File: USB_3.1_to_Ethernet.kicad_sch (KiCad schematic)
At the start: 5 parts, among them J1 RJ45_JK0654219, U1 LAN7801_9JX, U2 93LC56B_SN, U3 KSZ9031RNXCC, Y1 C3E-8.000-18-3030-R

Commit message: power section added and power conections made
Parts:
- Y1: value C3E-8.000-18-3030-R -> 125MHz
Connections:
- net DVDDH is gone; now on net AVDDH: U3.16 (DVDDH), U3.34 (DVDDH), U3.40 (DVDDH)
- net DVDDL is gone; now on net AVDDL: U3.14 (DVDDL), U3.18 (DVDDL), U3.23 (DVDDL), U3.26 (DVDDL), U3.30 (DVDDL), U3.39 (DVDDL)
- net P_GND is gone; now on net GND: U3.49 (P_GND), U3.49_1 (P_GND), U3.49_10 (P_GND), U3.49_11 (P_GND), U3.49_12 (P_GND), U3.49_13 (P_GND), U3.49_14 (P_GND), U3.49_15 (P_GND), U3.49_16 (P_GND), U3.49_17 (P_GND), U3.49_18 (P_GND), U3.49_19 (P_GND), U3.49_2 (P_GND), U3.49_20 (P_GND), U3.49_21 (P_GND), U3.49_22 (P_GND), U3.49_23 (P_GND), U3.49_24 (P_GND), U3.49_25 (P_GND), U3.49_3 (P_GND), U3.49_4 (P_GND), U3.49_5 (P_GND), U3.49_6 (P_GND), U3.49_7 (P_GND), U3.49_8 (P_GND), U3.49_9 (P_GND)
- net VDDVARIO is gone; now on net AVDDH: U1.11 (VDDVARIO), U1.18 (VDDVARIO), U1.27 (VDDVARIO), U1.3 (VDDVARIO), U1.48 (VDDVARIO), U1.51 (VDDVARIO), U1.7 (VDDVARIO)
- net AVDDH: now also U1.21 (VDD_SW_IN), U1.50 (VDD33A), U1.64 (VDD33_REG_IN)
- net GND: now also U1.65 (VSS), U3.29 (VSS)
- net XI: now reaches Y1.1
- net XI: now also U1.52 (XI)
- net XO: now reaches Y1.3
- net XO: now also U1.53 (XO)
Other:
- moved on the sheet: U1, Y1

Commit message: usb connections done without 27 ohm, SMI connections done, EEPROM connections done.
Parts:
- added R1: 12K, Resistor_SMD:R_0201_0603Metric_Pad0.64x0.40mm_HandSolder, symbol Device:R
- added R2, R3: 1.5K, Resistor_SMD:R_1206_3216Metric, symbol Device:R
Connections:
- net AVDDH: now also U2.8 (VCC), R2.1, R3.1
- net GND: now also U2.5 (VSS), R1.2
- net CS: now reaches U2.1 (CS)
- net CS: now also U1.23 (EECS/GPIO0)
- net CLK: now reaches U2.2 (CLK)
- net CLK: now also U1.26 (EECLK/GPIO3)
- net DI: now reaches U2.3 (DI)
- net DI: now also U1.24 (EEDI/GPIO1)
- net DO: now reaches U2.4 (DO)
- net DO: now also U1.25 (EEDO/GPIO2)
- net MDC: now reaches U3.36 (MDC)
- net MDC: now also U1.56 (MDC), R2.2
- net MDIO: now reaches U3.37 (MDIO)
- net MDIO: now also U1.55 (MDIO), R3.2
- net D+: now reaches U1.38 (USB2_DP)
- net D-: now reaches U1.39 (USB2_DM)
- net SSTX+: now reaches U1.40 (USB3_TXDP)
- net SSTX-: now reaches U1.41 (USB3_TXDM)
- net SSRX+: now reaches U1.43 (USB3_RXDP)
- net SSRX-: now reaches U1.44 (USB3_RXDM)
- net at U1.49 (USBRBIAS): now also R1.1
- no-connect marks 0 -> 1
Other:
- note added: "Gigabit Ethernet MAC"
- note added: "clk circuitry"
- moved on the sheet: J1, U1, U2, U3, Y1

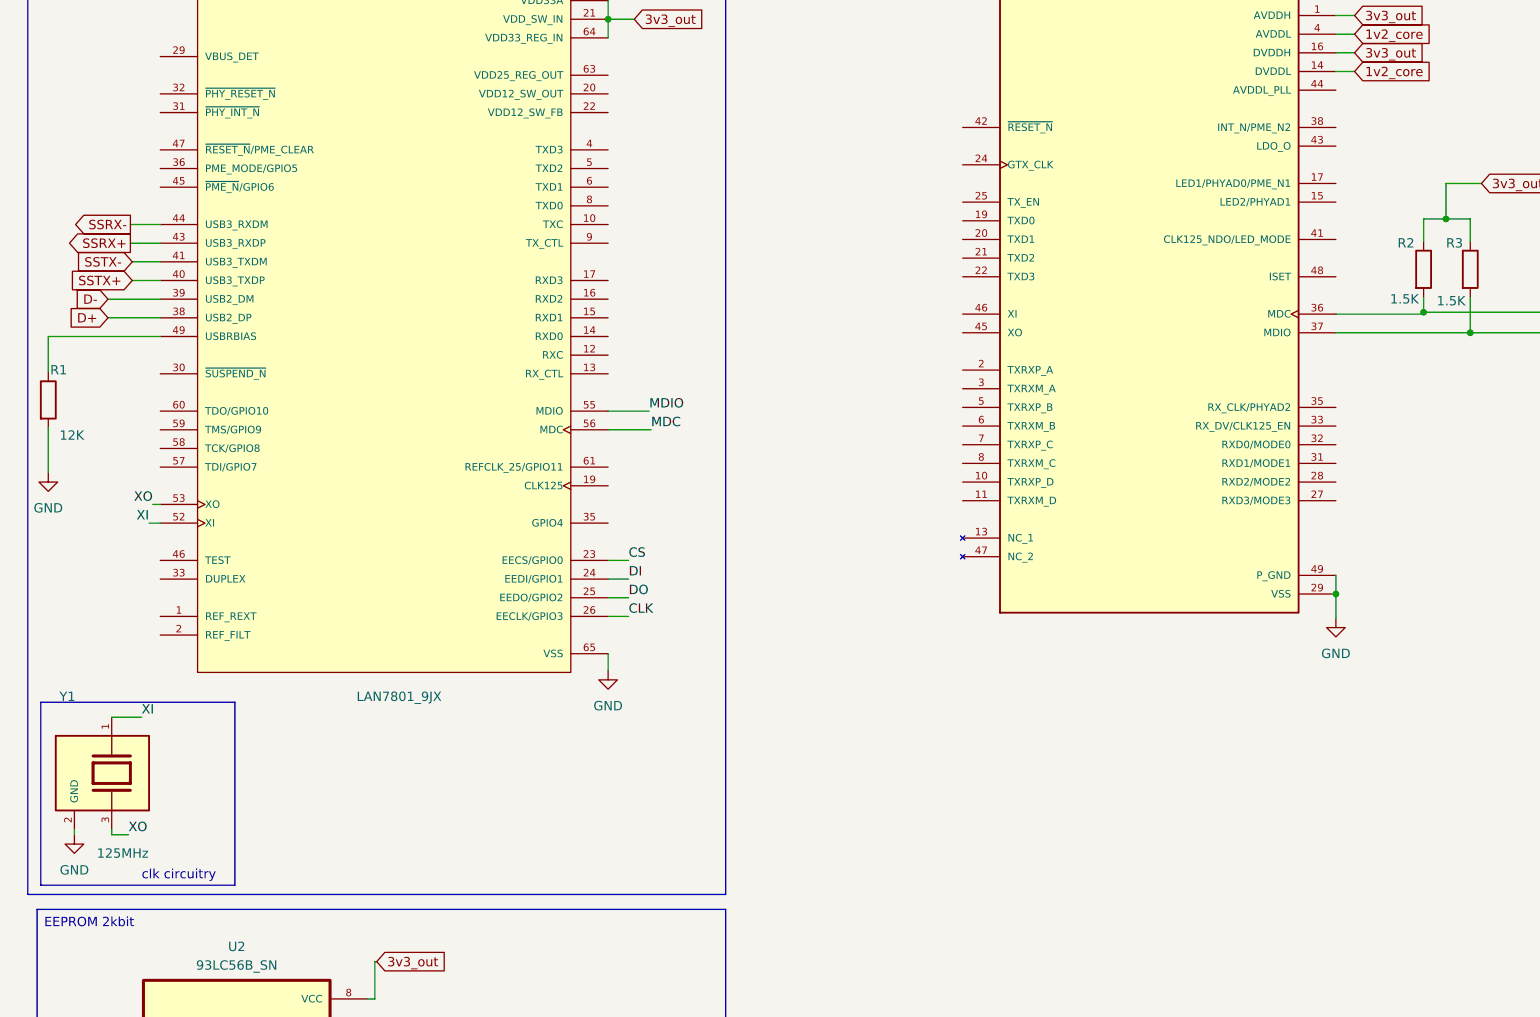
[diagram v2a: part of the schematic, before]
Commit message: RGMII connections made, Clk circuitry made, 27 ohm resistors added
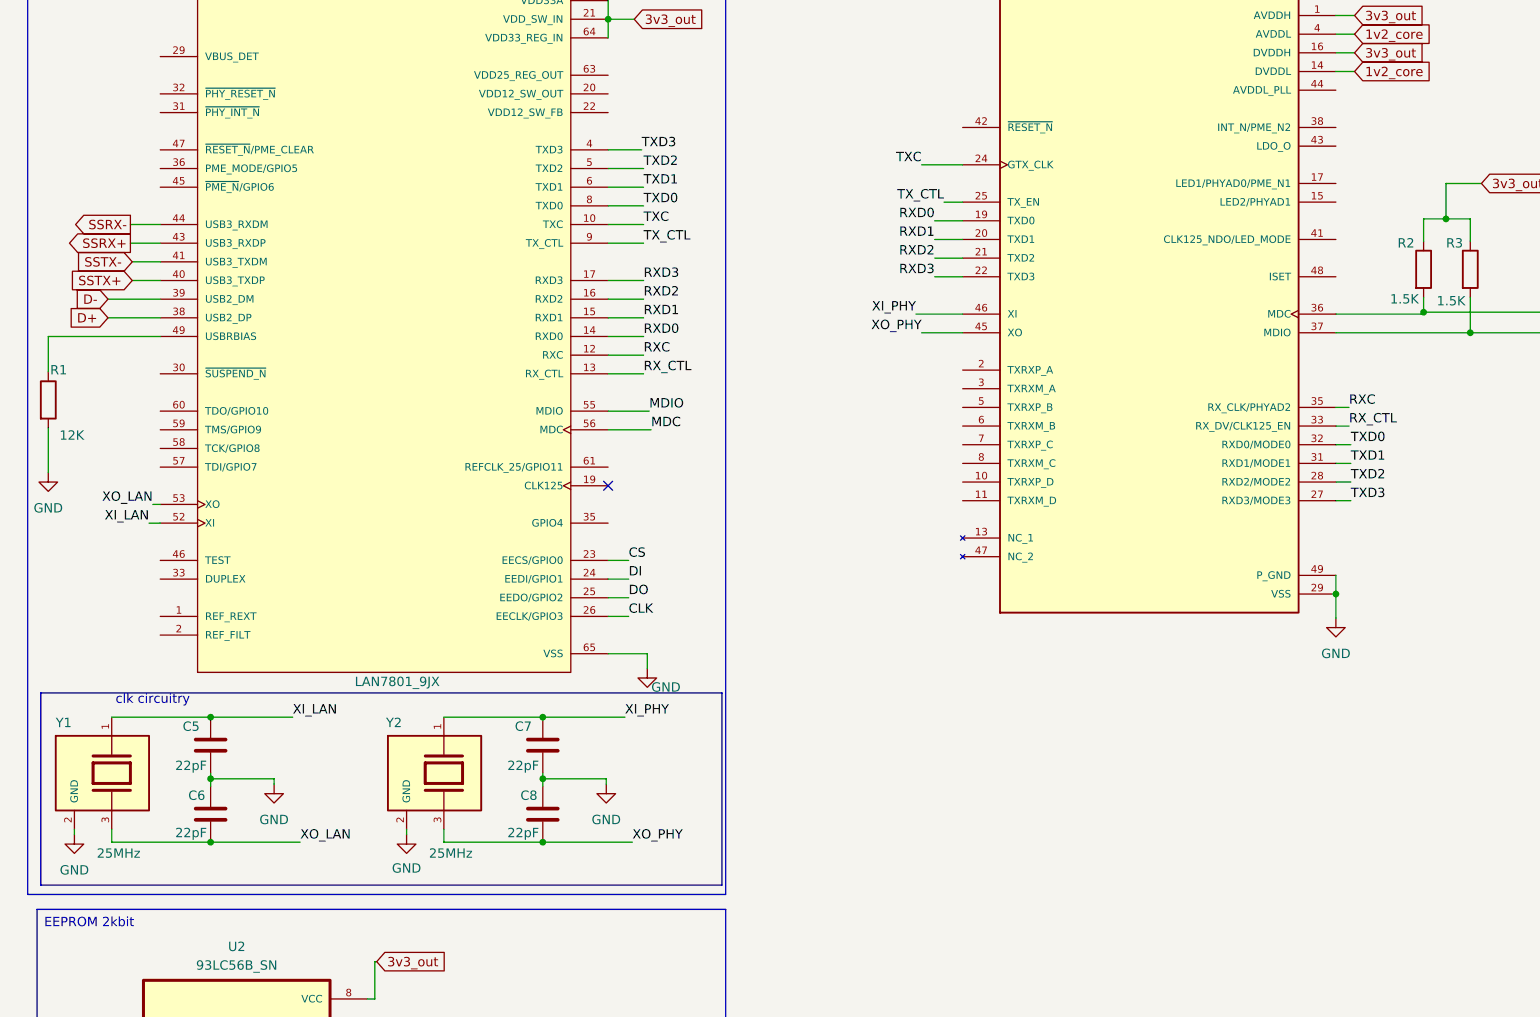
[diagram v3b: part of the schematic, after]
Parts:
- added C5, C6, C7, C8: 22pF, Capacitor_SMD:C_0603_1608Metric, symbol Device:C
- added Y2: 25MHz, Crystal:XTAL_ABMM325000MHZET, symbol C3E-8.000-18-3030-R:C3E-8.000-18-3030-R
- Y1: value 125MHz -> 25MHz; footprint C3E-8.000-18-3030-R:XTAL_C3E-8.000-18-3030-R -> Crystal:XTAL_ABMM325000MHZET
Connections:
- net GND: now also C5.2, C6.1, C7.2, C8.1, Y2.2 (GND), Y2.4 (GND)
- net RXD0: now reaches U3.19 (TXD0)
- net RXD0: now also U1.14 (RXD0)
- net RXD1: now reaches U3.20 (TXD1)
- net RXD1: now also U1.15 (RXD1)
- net RXD2: now reaches U3.21 (TXD2)
- net RXD2: now also U1.16 (RXD2)
- net RXD3: now reaches U3.22 (TXD3)
- net RXD3: now also U1.17 (RXD3)
- net TXC: now reaches U3.24 (GTX_CLK)
- net TXC: now also U1.10 (TXC)
- net TX_CTL: now reaches U3.25 (TX_EN)
- net TX_CTL: now also U1.9 (TX_CTL)
- net TXD3: now reaches U3.27 (RXD3/MODE3)
- net TXD3: now also U1.4 (TXD3)
- net TXD2: now reaches U3.28 (RXD2/MODE2)
- net TXD2: now also U1.5 (TXD2)
- net TXD1: now reaches U3.31 (RXD1/MODE1)
- net TXD1: now also U1.6 (TXD1)
- net TXD0: now reaches U3.32 (RXD0/MODE0)
- net TXD0: now also U1.8 (TXD0)
- net RX_CTL: now reaches U3.33 (RX_DV/CLK125_EN)
- net RX_CTL: now also U1.13 (RX_CTL)
- net RXC: now reaches U3.35 (RX_CLK/PHYAD2)
- net RXC: now also U1.12 (RXC)
- net XO_PHY: now reaches U3.45 (XO)
- net XO_PHY: now also C8.2, Y2.3
- net XI_PHY: now reaches U3.46 (XI)
- net XI_PHY: now also C7.1, Y2.1
- net XI renamed XI_LAN
- net XI_LAN: now also C5.1
- net XO renamed XO_LAN
- net XO_LAN: now also C6.2
- no-connect marks 1 -> 2

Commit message: Added 27R resistors to RGMII interface, added 0.1uF AC coupling caps on sstx/rx, Magjack connections done
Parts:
- added C13, C14, C15, C16: 0.1uF, Capacitor_SMD:C_1206_3216Metric_Pad1.33x1.80mm_HandSolder, symbol Device:C
- added R10, R11, R12, R13, R14, R15, R16, R17, R18, R19, R6, R7, R8, R9: 27R, Resistor_SMD:R_1206, symbol Device:R
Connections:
- net AVDDH: now also J1.14 (LED2+), J1.16 (LED1+)
- net GND: now also J1.SH, C13.1, C14.1, C15.1, C16.1
- net RXC: now also R14.1; no longer U3.35 (RX_CLK/PHYAD2)
- net RXD0: now also R11.1; no longer U3.19 (TXD0)
- net RXD1: now also R10.1; no longer U3.20 (TXD1)
- net RXD2: now also R13.1; no longer U3.21 (TXD2)
- net RXD3: now also R12.1; no longer U3.22 (TXD3)
- net RX_CTL: now also R15.1; no longer U3.33 (RX_DV/CLK125_EN)
- net TXC: now also R16.1; no longer U3.24 (GTX_CLK)
- net TXD0: now also U3.19 (TXD0), R9.1, R9.2; no longer U3.32 (RXD0/MODE0)
- net TXD1: now also U3.20 (TXD1), R8.1, R8.2; no longer U3.31 (RXD1/MODE1)
- net TXD2: now also U3.21 (TXD2), R7.1, R7.2; no longer U3.28 (RXD2/MODE2)
- net TXD3: now also U3.22 (TXD3), R6.1, R6.2; no longer U3.27 (RXD3/MODE3)
- net TX_CTL: now also R17.1; no longer U3.25 (TX_EN)
- net TXRXP_D: now reaches U3.10 (TXRXP_D)
- net TXRXP_D: now also J1.8 (MX4+)
- net TXRXM_D: now reaches U3.11 (TXRXM_D)
- net TXRXM_D: now also J1.9 (MX4-)
- net LED2/PHYAD1: now reaches U3.15 (LED2/PHYAD1)
- net LED2/PHYAD1: now also R19.1
- net LED1/PHYAD0/PME_N1: now reaches U3.17 (LED1/PHYAD0/PME_N1)
- net LED1/PHYAD0/PME_N1: now also R18.1
- net TXRXP_A: now reaches U3.2 (TXRXP_A)
- net TXRXP_A: now also J1.11 (MX1+)
- net TXRXM_A: now reaches U3.3 (TXRXM_A)
- net TXRXM_A: now also J1.10 (MX1-)
- net TXRXP_B: now reaches U3.5 (TXRXP_B)
- net TXRXP_B: now also J1.4 (MX2+)
- net TXRXM_B: now reaches U3.6 (TXRXM_B)
- net TXRXM_B: now also J1.5 (MX2-)
- net TXRXP_C: now reaches U3.7 (TXRXP_C)
- net TXRXP_C: now also J1.3 (MX3+)
- net TXRXM_C: now reaches U3.8 (TXRXM_C)
- net TXRXM_C: now also J1.2 (MX3-)
- net at J1.1 (MXCT3): now also C15.2
- net at J1.12 (MXCT1): now also C13.2
- net LED2-: now reaches J1.13 (LED2-)
- net LED2-: now also R19.2
- net LED1-: now reaches J1.15 (LED1-)
- net LED1-: now also R18.2
- net at J1.6 (MXCT2): now also C14.2
- net at J1.7 (MXCT4): now also C16.2
- new net GTX_CLK: R17.2, U3.24 (GTX_CLK)
- new net RXD0/MODE0: R11.2, U3.32 (RXD0/MODE0)
- new net RXD1/MODE1: R10.2, U3.31 (RXD1/MODE1)
- new net RXD2/MODE2: R13.2, U3.28 (RXD2/MODE2)
- new net RXD3/MODE3: R12.2, U3.27 (RXD3/MODE3)
- new net RX_CLK/PHYAD2: U3.35 (RX_CLK/PHYAD2)
- new net RX_CLK/PHYAD2: R14.2
- new net RX_DV/CLK125_EN: R15.2, U3.33 (RX_DV/CLK125_EN)
- new net TX_EN: R16.2, U3.25 (TX_EN)
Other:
- note added: "MAC side"
- note added: "PHY side"
- moved on the sheet: J1, R2, R3, U3

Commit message: no major changes, APll tied to 3v3
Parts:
- R1: footprint Resistor_SMD:R_0201_0603Metric_Pad0.64x0.40mm_HandSolder -> Capacitor_SMD:C_01005_0402Metric
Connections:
- net VDD12A is gone; now on net AVDDL: U1.37 (VDD12A), U1.42 (VDD12A), U1.62 (VDD12A)
- net AVDDL: now also U3.44 (AVDDL_PLL)
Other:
- moved on the sheet: C13, C14, C15, C6, C7, C8, R1, R10, R11, R12, R13, R14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

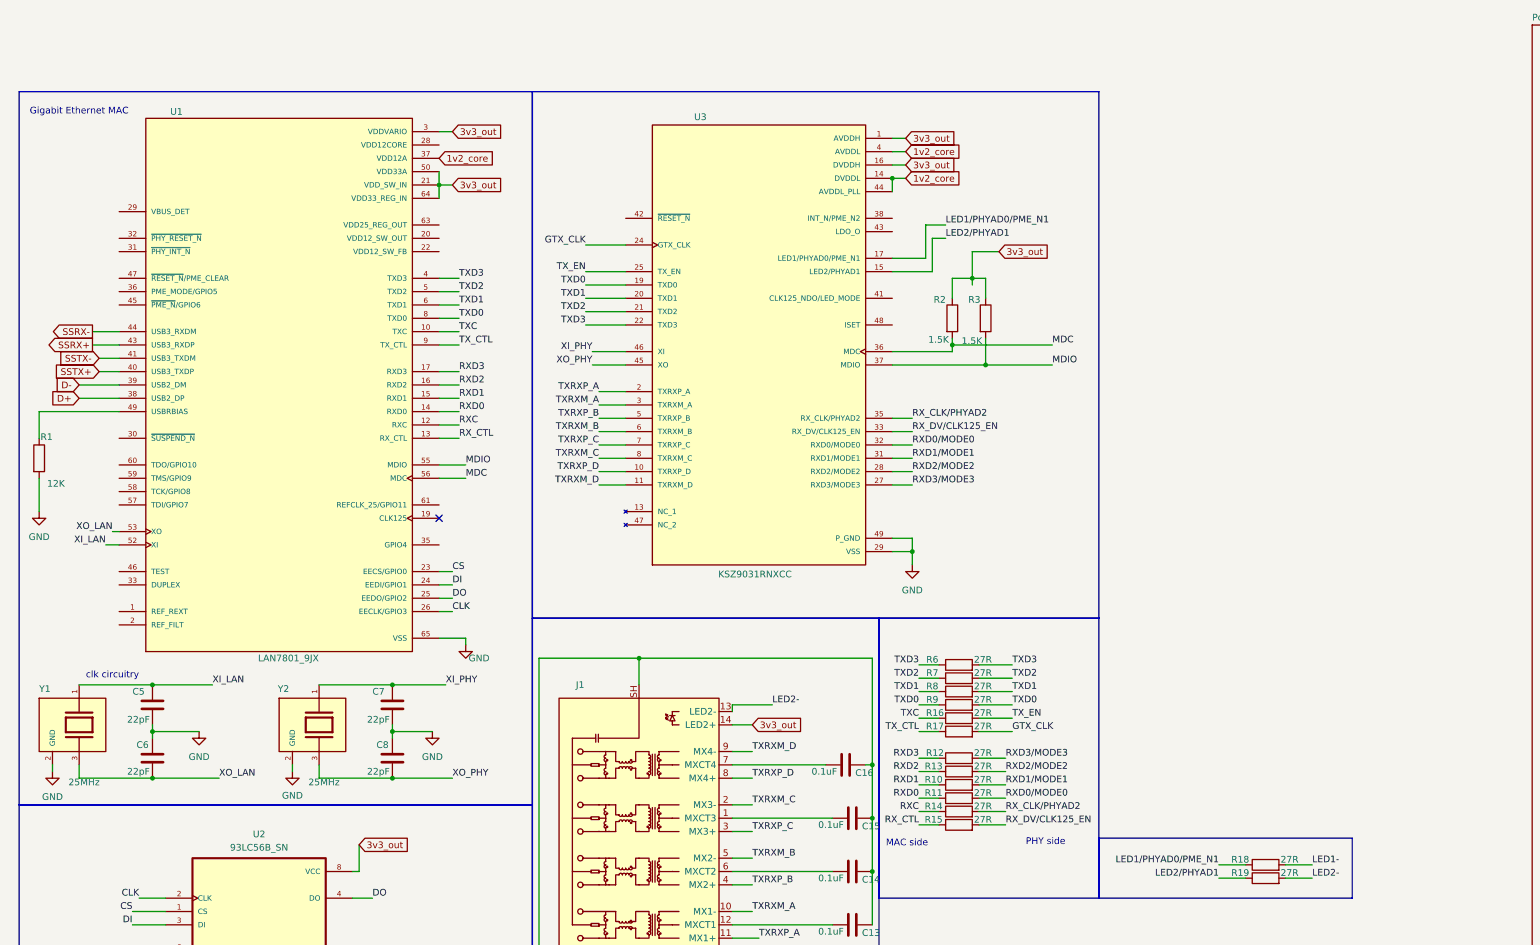
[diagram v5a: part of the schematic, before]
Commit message: 1. Decoupling capacitors for Lan7801 ic added 2. 3.3v Input given to TPS7A0212 instead of 5v 3. Ref+Rfilt resistor capacitor added 4. Iset resistor 12K added 5. Test Pull-down and Duplex Pull-up 10K added
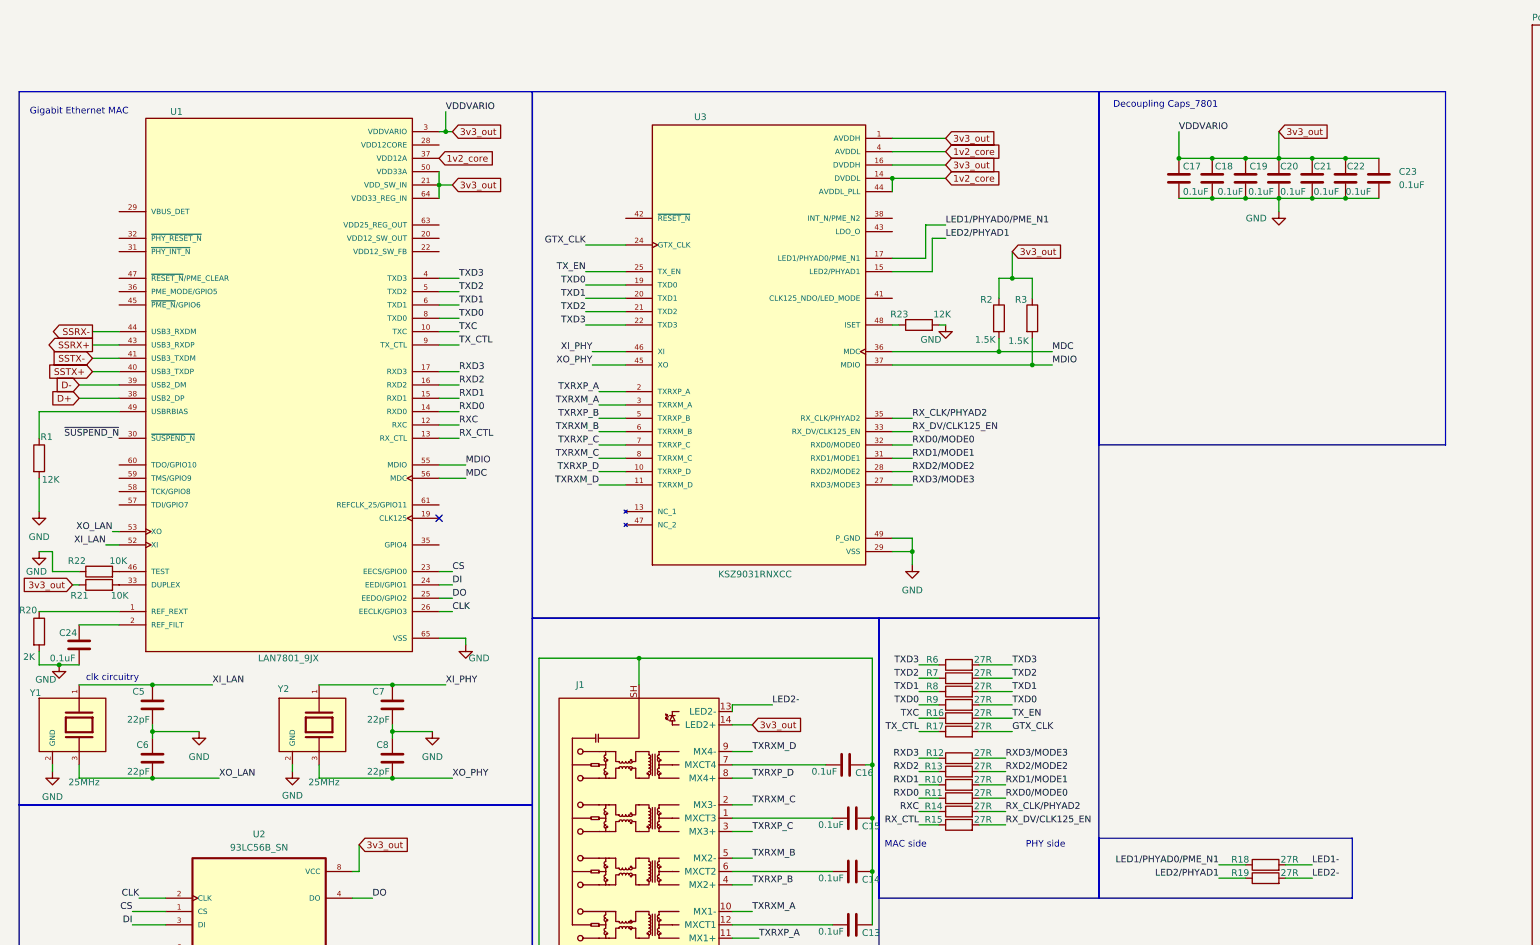
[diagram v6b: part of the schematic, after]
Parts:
- added C17, C18, C19, C20, C21, C22, C23, C24: 0.1uF, Capacitor_SMD:C_01005_0402Metric, symbol Device:C
- added R20: 2K, Capacitor_SMD:C_01005_0402Metric, symbol Device:R
- added R21, R22: 10K, Capacitor_SMD:C_01005_0402Metric, symbol Device:R
- added R23: 12K, Capacitor_SMD:C_01005_0402Metric, symbol Device:R
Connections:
- net AVDDH: now also C17.1, C18.1, C19.1, C20.1, C21.1, C22.1, C23.1, R21.1
- net GND: now also C17.2, C18.2, C19.2, C20.2, C21.2, C22.2, C23.2, C24.2, R20.2, R22.1, R23.2
- net at U3.48 (ISET): now also R23.1
- net at U1.1 (REF_REXT): now also R20.1
- net at U1.2 (REF_FILT): now also C24.1
- net ~{SUSPEND_N}: now reaches U1.30 (~{SUSPEND_N})
- net at U1.33 (DUPLEX): now also R21.2
- net at U1.46 (TEST): now also R22.2
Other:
- note added: "Decoupling Caps_7801"
- moved on the sheet: R2, R3
